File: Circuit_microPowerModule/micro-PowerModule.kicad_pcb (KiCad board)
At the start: 2 copper layers, 163.7 x 124.2 mm, 235 parts, among them J101 Screw_Terminal_01x02, J102 Jack-DC, J201 USB_C_Receptacle_USB2.0, J202 Debug, J401 Conn_01x03, J402 Screw_Terminal_01x02, J403 Screw_Terminal_01x02, J404 Screw_Terminal_01x02, J501 HDR-2.54 Male 1x5, J502 MikroBus, J503 HDR-2.54 Female 1x5, Q301 MMBT3906, Q302 RK7002BM, Q303 IRF5305S, Q401 RU1C002ZP, Q402 RK7002BM, Q403 RU1C002ZP, Q404 RK7002BM, Q501 S8550, SW201 KMR2, SW301 SW_DPDT_x2, SW501 RotaryEncoder_Switch, U201 W25Q128JVS, U202 RP2040, U204 USBLC6-2P6, U301 OPA376xxDBV, U302 MP2315S, U401 MP2315S, U402 MCP4725xxx-xCH, U403 MT3608, U404 OPA376xxDBV, U405 MCP4725xxx-xCH, U406 INA219BxD, U407 L298N, U408 OPA376xxDBV, U501 MAX485E, Y201 12MHz

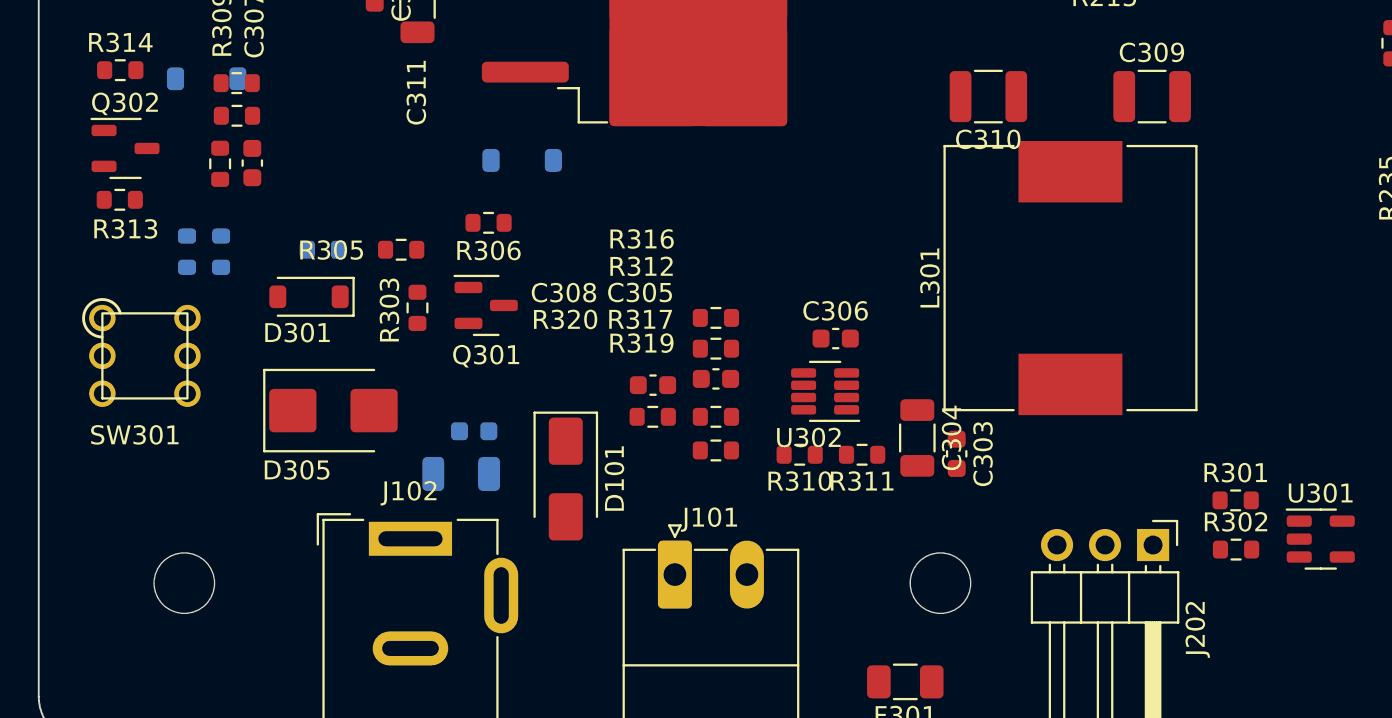
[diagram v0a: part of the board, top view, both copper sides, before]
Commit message: update U302 PCB Layout
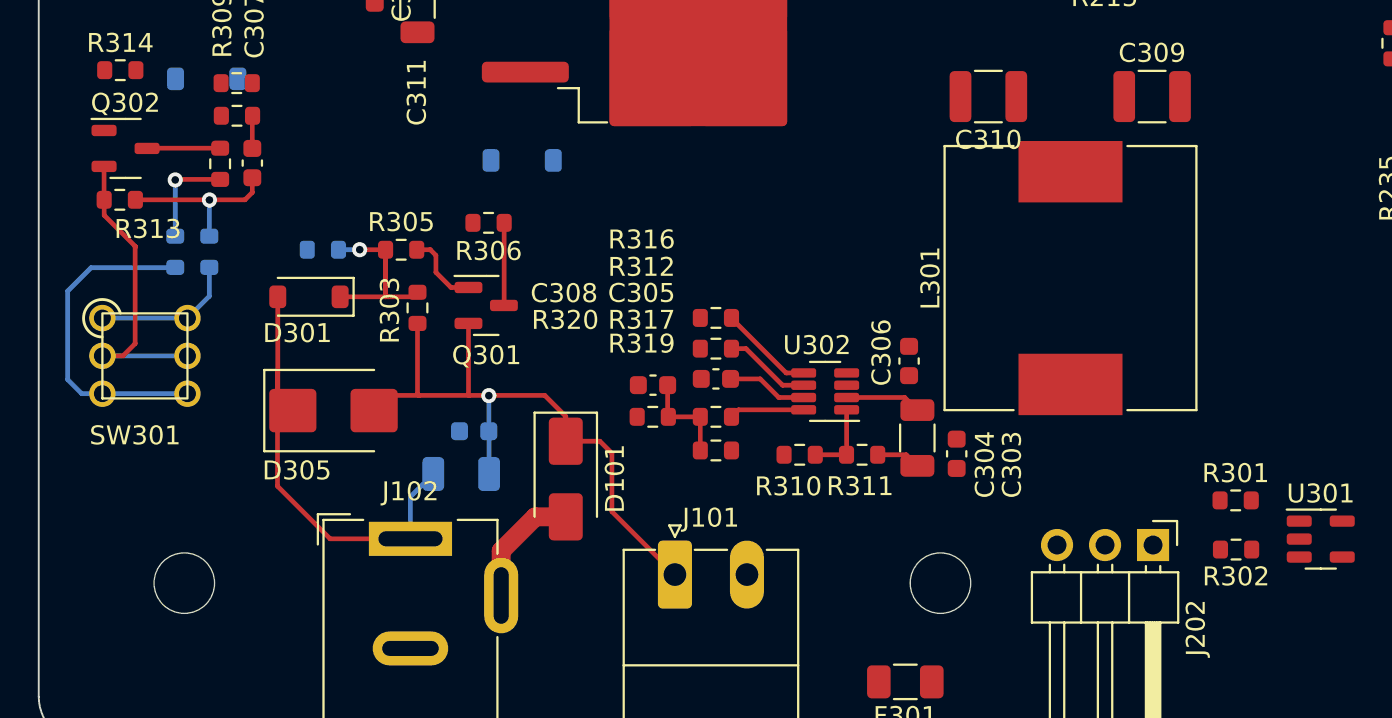
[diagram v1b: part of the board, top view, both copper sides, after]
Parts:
- moved C306 4.06 mm to (93.3, 143.2), turned to -90 degrees
- moved R308 2.43 mm to (54.5, 137.5)
- moved R307 1.18 mm to (56.3, 137.5)
- turned R302 to 180 degrees
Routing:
- net /PWR_IN: track 0.00 -> 43.6 mm, vias 0 -> 2
- net GNDPWR: track 0.00 -> 32.2 mm, vias 0 -> 1
- net Net-(SW301A-C): track 0.00 -> 17.5 mm
- net Net-(Q302-G): track 0.00 -> 16.6 mm
- net Net-(D301-K): track 0.00 -> 11.5 mm, vias 0 -> 1
- net Net-(SW301A-A): track 0.00 -> 7.66 mm
- net Net-(D101-A): track 0.00 -> 6.52 mm
- net Net-(C308-Pad1): track 0.00 -> 5.16 mm
- net Net-(U302-BST): track 0.00 -> 5.03 mm
- net Net-(U302-EN): track 0.00 -> 4.62 mm
- net Net-(Q301-C): track 0.00 -> 4.37 mm
- net Net-(U302-VCC): track 0.00 -> 4.27 mm
- net Net-(Q301-B): track 0.00 -> 4.09 mm
- net Net-(U302-AAM): track 0.00 -> 4.03 mm
- net +VDC: track 0.00 -> 4.01 mm
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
